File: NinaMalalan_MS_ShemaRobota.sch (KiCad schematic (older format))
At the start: 29 parts

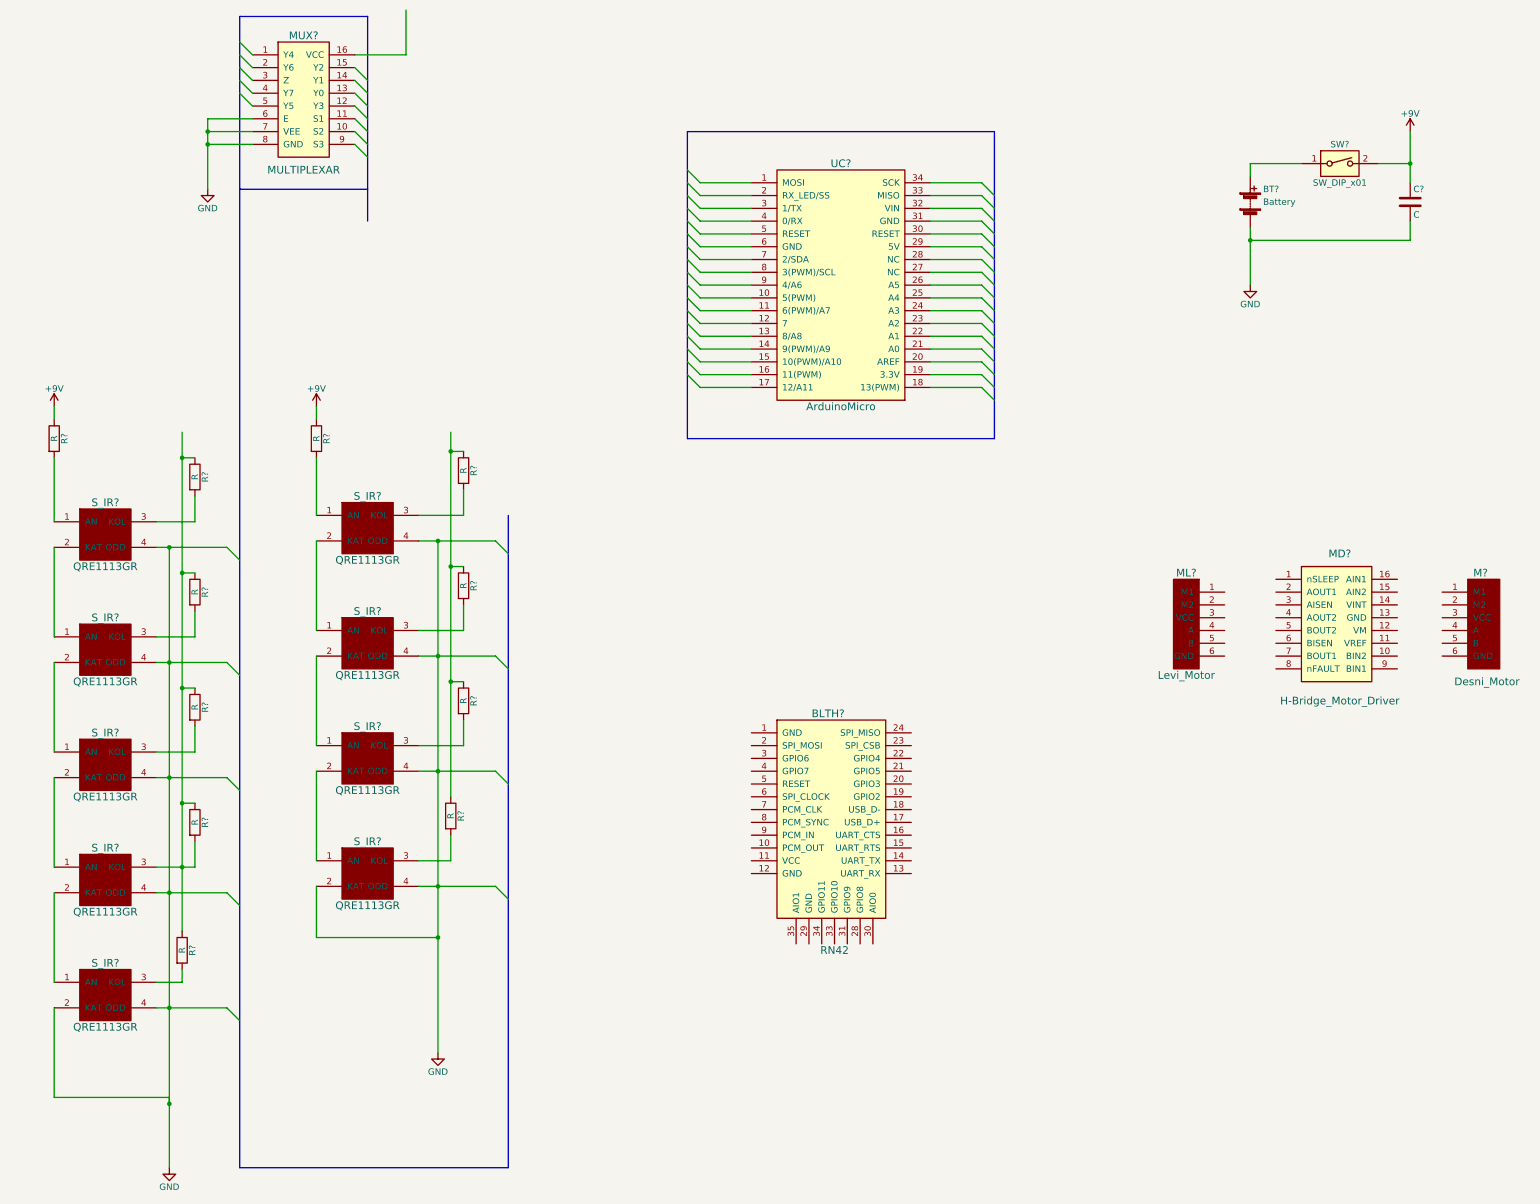
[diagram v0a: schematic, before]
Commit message: NADALJEVANJE VEZANJA
Še vedno ni zaključeno... manjkajo vse veličine in oznake
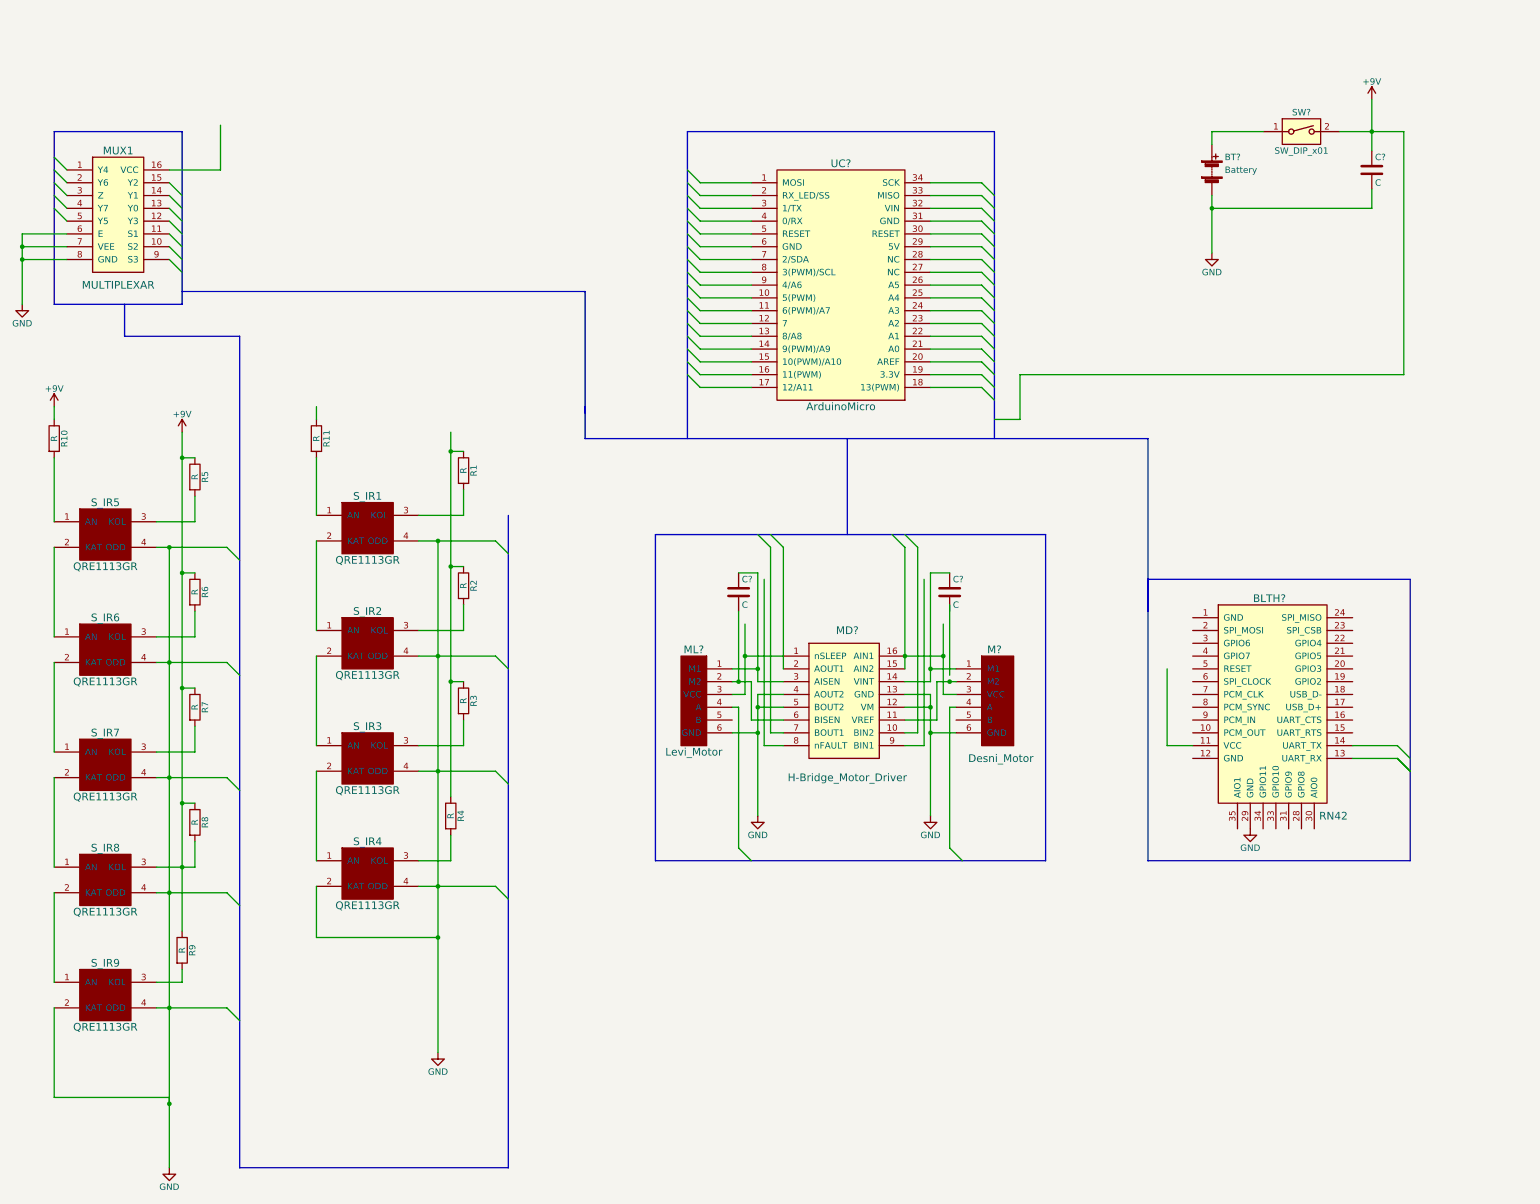
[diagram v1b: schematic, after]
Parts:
- added C? (x2): C, symbol C
- gave numbers to parts that had none: 21
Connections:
- wire segments 101 -> 153
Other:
- moved on the sheet: BLTH?, BT?, C?, M?, MD?, ML?, MUX1, SW?
